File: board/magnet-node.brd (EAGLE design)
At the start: 22.9 x 23.1 mm, 30 parts, among them X1 SMA-142-0701-801/806, X2 SMA-142-0711-821/826

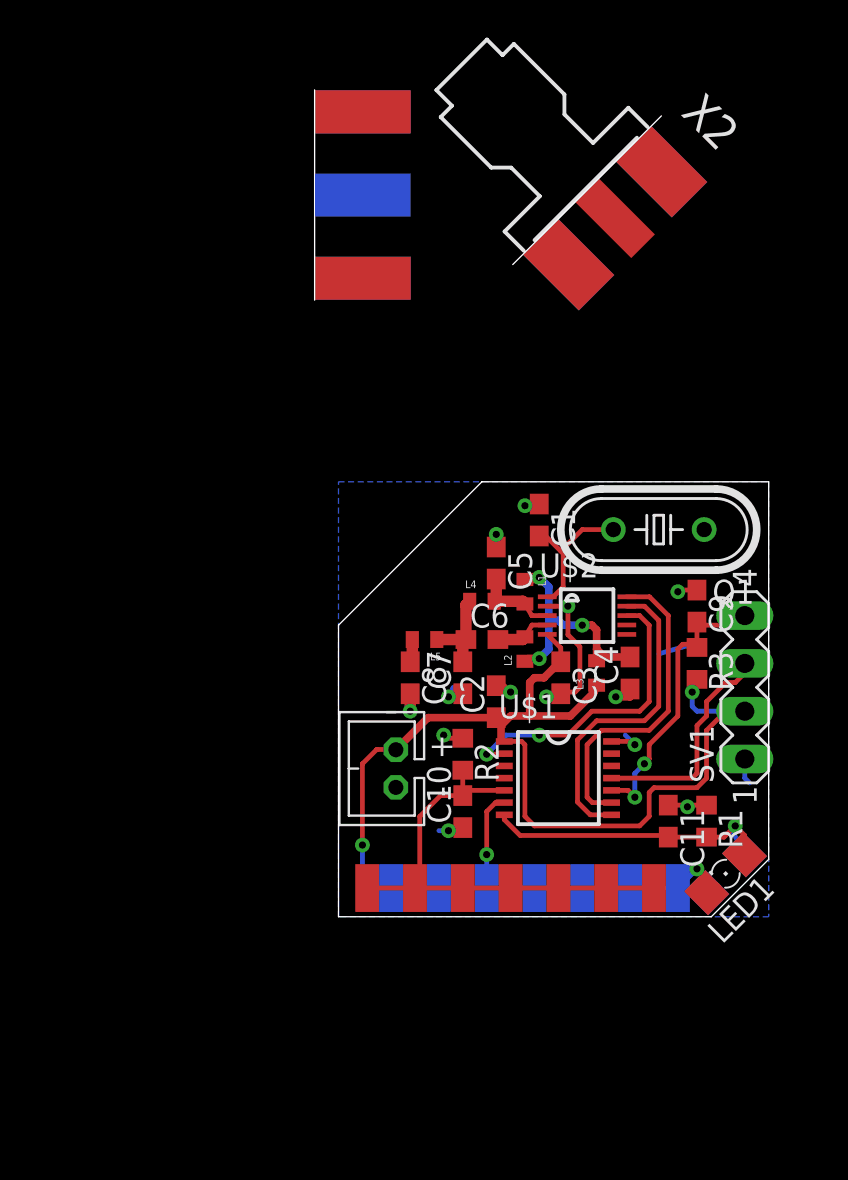
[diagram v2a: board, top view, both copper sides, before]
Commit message: added temp/humid sensor
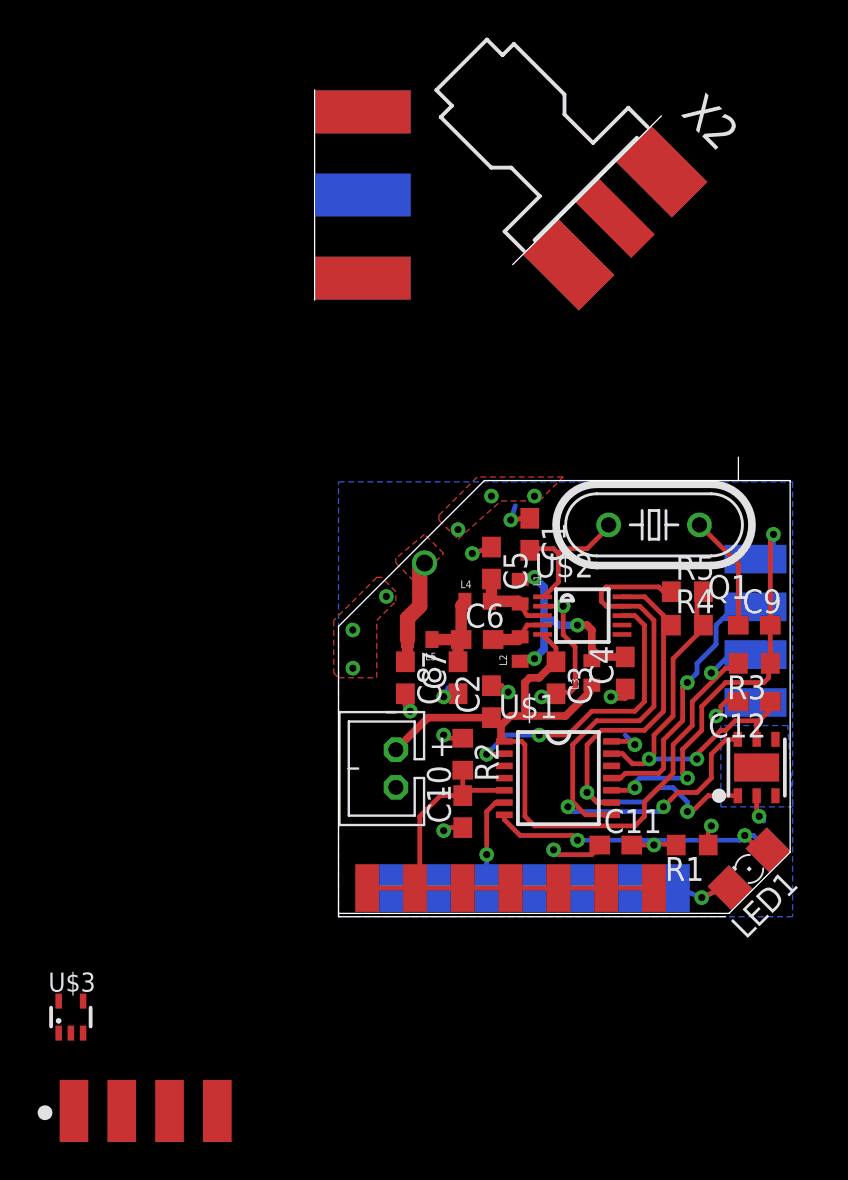
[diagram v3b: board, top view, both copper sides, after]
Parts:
- added C12: (no value), rcl:C0603
- added IC1: HTU21D, Mine:DFN6-L
- added R4, R5: (no value), rcl:R0603
- added SV4: (no value), Mine:EDGE_4
- added U$3: LMT85, Mine:SC70-5L
- SV1: device con-lstb:MA04-1 -> Mine:EDGE_4
- moved C9 3.21 mm to (22.1, 20.1), turned to 0 degrees
- moved C11 3.07 mm to (14.7, 8.38), turned to 0 degrees
- moved SV1 3.06 mm to (22.2, 19.8), flipped to the bottom
- moved R3 3.05 mm to (22.1, 18.0), turned to 180 degrees
- moved R1 1.48 mm to (18.8, 8.38), turned to 180 degrees
- moved LED1 1.28 mm to (21.8, 7.11)
- moved LED2 1.28 mm to (21.8, 7.11)
- moved C1 0.91 mm to (10.2, 24.9)
- moved Q1 0.35 mm to (16.8, 25.4)
- moved L1 0.25 mm to (9.65, 21.8)
- moved L2 0.25 mm to (9.65, 18.8)
- moved C6 0.25 mm to (7.37, 19.3)
- moved C7 0.25 mm to (6.35, 17.3)
- moved L4 0.25 mm to (7.37, 21.3)
- moved L5 0.25 mm to (4.32, 19.3)
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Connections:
- removed net N$3: U$1.8, U$2.9
- removed net N$6: U$1.9, U$2.10
- new net N$11: U$1.3
- new net N$14: U$1.4
- new net SCL: IC1.6, R5.1, U$1.8, U$2.9
- new net SDA: IC1.1, R4.1, U$1.9, U$2.10
- new net VCCS2: C12.1, IC1.5, R4.2, R5.2, U$1.13
- net GND: now also C12.2, IC1.2
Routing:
- net SCL: track 0.00 -> 34.6 mm, vias 0 -> 2
- net SDA: track 0.00 -> 26.8 mm, vias 0 -> 2
- net VCCS2: track 0.00 -> 22.1 mm, vias 0 -> 2
- net N$3: track 17.0 -> 0.00 mm
- net N$6: track 17.0 -> 0.00 mm
- net +3V3: track 55.1 -> 45.0 mm, vias 2 -> 1
- net GND: track 24.9 -> 34.0 mm, vias 13 -> 21
- net N$15: track 15.8 -> 23.1 mm, vias 2 -> 3
- net N$10: track 1.23 -> 5.56 mm, vias 0 -> 1
- net N$2: track 11.8 -> 14.2 mm, vias 0 -> 1
- net N$13: track 17.3 -> 19.4 mm, vias 1 -> 3
- net VCCS: track 26.1 -> 26.9 mm
- added copper zone on layer 1, net GND
- added copper zone on layer 1, net N$10
- added copper zone on layer 16, net N$3
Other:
- board size 22.9 x 23.1 mm -> 24 x 24.4 mm

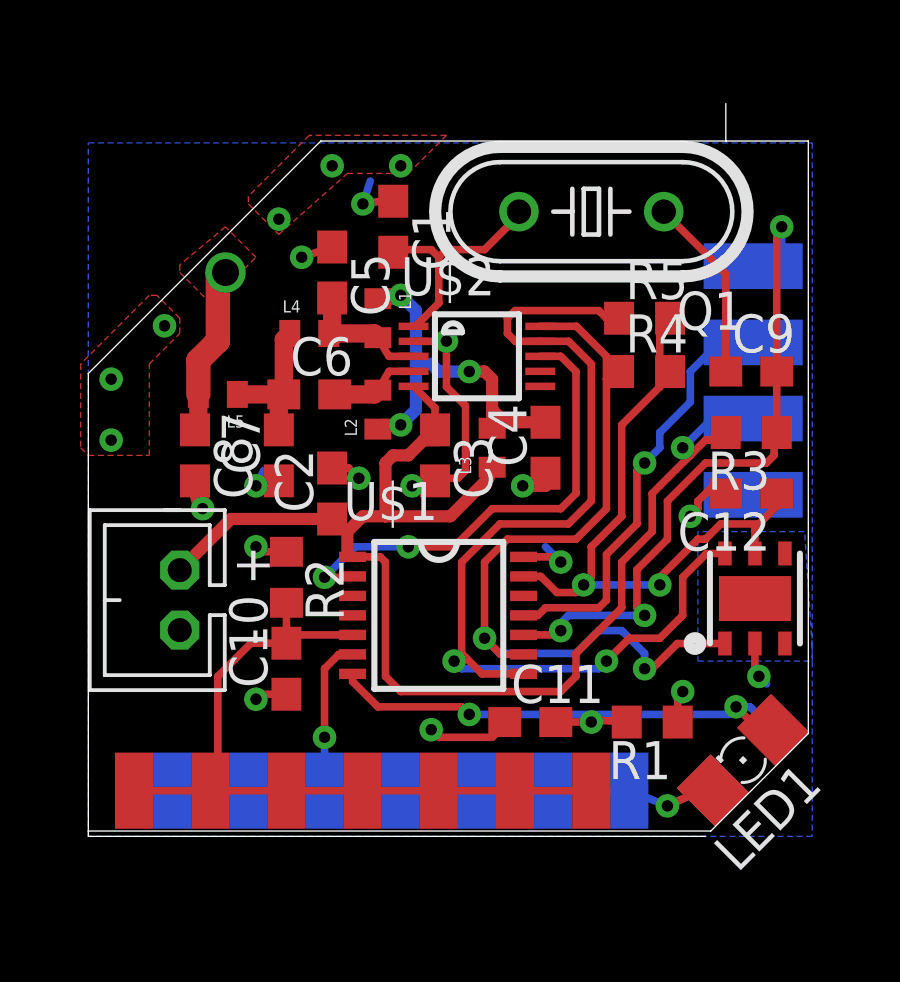
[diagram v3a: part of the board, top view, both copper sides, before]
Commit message: changed footprints in magnet node
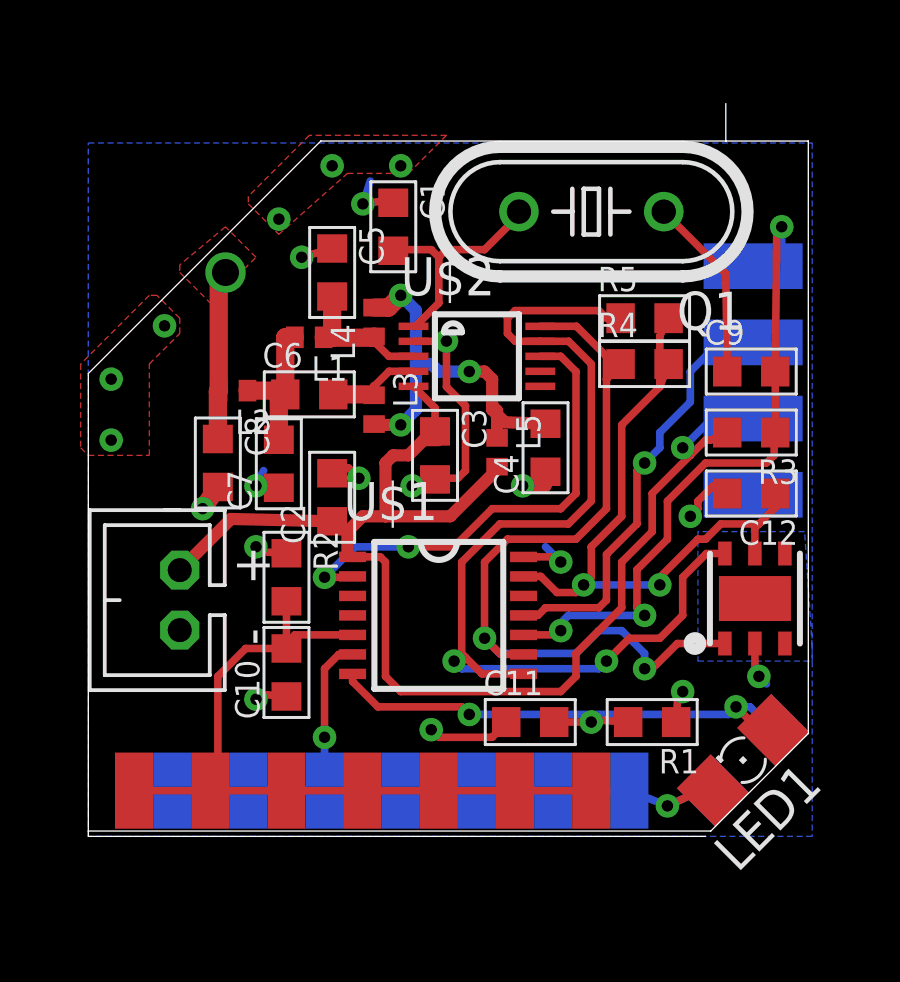
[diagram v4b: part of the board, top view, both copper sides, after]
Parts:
- C1, C10, C11, C12, C2, C3, C4, C5, C6, C7, C8, C9: device rcl:C0603 -> passives-7351:C0603-N
- L1, L2, L3, L4, L5: device SparkFun-Passives:C0402 -> passives-7351:L0402-N
- R1, R2, R3, R4, R5: device rcl:R0603 -> passives-7351:R0603-N
- moved L5 9.50 mm to (13.6, 17.4), turned to 270 degrees
- moved L2 4.87 mm to (4.83, 19.4), turned to 180 degrees
- moved L3 4.14 mm to (9.53, 18.8), turned to 270 degrees
- moved L1 2.37 mm to (7.37, 21.2), turned to 180 degrees
- moved L4 2.19 mm to (9.53, 21.7), turned to 90 degrees
- moved C8 0.80 mm to (4.32, 17.0)
- moved C7 0.28 mm to (6.35, 17.0)
- moved R4 0.25 mm to (18.5, 20.3)
- moved C2 0.13 mm to (8.13, 15.9)
- moved C10 0.12 mm to (6.60, 10.0)
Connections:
- net +3V3: now also L5.2; no longer L3.1
- net N$10: now also L2.2; no longer L5.2
- net N$4: now also L4.2, L5.1; no longer L1.1, L2.1
- net N$7: now also L1.2, L2.1; no longer L4.1, L5.1
- net N$8: now also L1.1, L4.1; no longer L1.2, L4.2
- net N$9: now also L3.1; no longer L2.2
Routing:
- net N$4: track 12.7 -> 13.4 mm

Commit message: adding some values and labels
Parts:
- C4, C5: value (none) -> 2.4p
- C6: value (none) -> 1.2p
- C7, C8: value (none) -> 5.1p
- L1: value (none) -> 30n
- L2: value (none) -> 6.8n
- L3, L4: value (none) -> 3.6n
- L5: value (none) -> 120n
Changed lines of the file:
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@@
 <element name="C1" library="passives-7351" package="C0603-N" value="" x="10.164" y="24.892" rot="R270"/>
 <element name="J2" library="dtb" package="JST-2-TH" value="" x="3.048" y="12.446" rot="R90"/>
-<element name="C4" library="passives-7351" package="C0603-N" value="" x="15.24" y="17.526" rot="R90"/>
-<element name="C5" library="passives-7351" package="C0603-N" value="" x="8.128" y="23.368" rot="R270"/>
-<element name="C6" library="passives-7351" package="C0603-N" value="" x="7.366" y="19.304"/>
-<element name="C7" library="passives-7351" package="C0603-N" value="" x="6.35" y="16.9926" rot="R90"/>
-<element name="C8" library="passives-7351" package="C0603-N" value="" x="4.318" y="17.018" rot="R270"/>
+<element name="C4" library="passives-7351" package="C0603-N" value="2.4p" x="15.24" y="17.526" rot="R90"/>
+<element name="C5" library="passives-7351" package="C0603-N" value="2.4p" x="8.128" y="23.368" rot="R270"/>
+<element name="C6" library="passives-7351" package="C0603-N" value="1.2p" x="7.366" y="19.304"/>
+<element name="C7" library="passives-7351" package="C0603-N" value="5.1p" x="6.35" y="16.9926" rot="R90"/>
+<element name="C8" library="passives-7351" package="C0603-N" value="5.1p" x="4.318" y="17.018" rot="R270"/>
 <element name="X1" library="con-coax" package="J502-ND-142-0701-801/806" value="SMA-142-0701-801/806" x="-1.27" y="42.926" rot="MR180">
 <attribute name="OC_NEWARK" value="90F2624" x="41.91" y="53.086" size="1.778" layer="28" rot="MR180" display="off"/>
@@
 <element name="R4" library="passives-7351" package="R0603-N" value="" x="18.542" y="20.316"/>
 <element name="R5" library="passives-7351" package="R0603-N" value="" x="18.542" y="21.844"/>
-<element name="L1" library="passives-7351" package="L0402-N" value="" x="7.366" y="21.209" rot="R180"/>
-<element name="L2" library="passives-7351" package="L0402-N" value="" x="4.826" y="19.431" rot="R180"/>
-<element name="L3" library="passives-7351" package="L0402-N" value="" x="9.525" y="18.796" rot="R270"/>
-<element name="L4" library="passives-7351" package="L0402-N" value="" x="9.525" y="21.717" rot="R90"/>
-<element name="L5" library="passives-7351" package="L0402-N" value="" x="13.625" y="17.375" rot="R270"/>
+<element name="L1" library="passives-7351" package="L0402-N" value="30n" x="7.366" y="21.209" rot="R180"/>
+<element name="L2" library="passives-7351" package="L0402-N" value="6.8n" x="4.826" y="19.431" rot="R180"/>
+<element name="L3" library="passives-7351" package="L0402-N" value="3.6n" x="9.525" y="18.796" rot="R270"/>
+<element name="L4" library="passives-7351" package="L0402-N" value="3.6n" x="9.525" y="21.717" rot="R90"/>
+<element name="L5" library="passives-7351" package="L0402-N" value="120n" x="13.625" y="17.375" rot="R270"/>
 </elements>
 <signals>

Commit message: small changes
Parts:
- removed SV4: (no value), Mine:EDGE_4
- added TP1, TP4: TPTP14SQ, testpad:TP14SQ
- L5: device passives-7351:L0402-N -> passives-7351:L0603-N
- moved R2 4.96 mm to (5.46, 8.38), turned to 180 degrees
- moved C10 4.62 mm to (2.29, 8.38), turned to 0 degrees
- moved L5 0.29 mm to (13.3, 17.4)
- moved C3 0.13 mm to (11.6, 17.4)
- moved C4 0.13 mm to (15.2, 17.4)
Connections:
- net N$11: now also TP1.TP
- net N$14: now also TP4.TP
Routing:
- net N$11: track 0.00 -> 2.76 mm
- net N$14: track 0.00 -> 2.51 mm
- net N$12: track 26.0 -> 25.1 mm
- net N$4: track 13.4 -> 12.9 mm

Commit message: removed power control from dht
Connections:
- net +3V3: now also C12.1, IC1.5, R4.2, R5.2
- net VCCS2: no longer C12.1, IC1.5, R4.2, R5.2
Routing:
- net VCCS2: track 22.3 -> 11.6 mm
- net +3V3: track 45.3 -> 49.8 mm
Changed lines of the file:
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@@
 <contactref element="L5" pad="2"/>
 <wire x1="13.335" y1="16.599" x2="13.625" y2="16.8" width="0.4064" layer="1"/>
+<contactref element="R4" pad="2"/>
+<contactref element="R5" pad="2"/>
+<contactref element="C12" pad="1"/>
+<contactref element="IC1" pad="5"/>
+<wire x1="19.342" y1="21.844" x2="19.342" y2="20.316" width="0.254" layer="1"/>
+<wire x1="19.342" y1="20.316" x2="19.342" y2="17.996" width="0.254" layer="1"/>
+<wire x1="19.342" y1="17.996" x2="19.812" y2="17.526" width="0.254" layer="1"/>
+<wire x1="22.22" y1="14" x2="22.898" y2="16.002" width="0" layer="19" extent="1-1"/>
+<wire x1="22.16" y1="18.498" x2="22.898" y2="16.002" width="0" layer="19" extent="1-16"/>
 </signal>
 <signal name="N$2">
@@
 <signal name="VCCS2">
 <contactref element="U$1" pad="13"/>
-<contactref element="C12" pad="1"/>
-<contactref element="IC1" pad="5"/>
 <wire x1="14.509" y1="13.238" x2="15.083" y2="13.238" width="0.254" layer="1"/>
 <wire x1="15.083" y1="13.238" x2="15.621" y2="12.7" width="0.254" layer="1"/>
@@
 <via x="19.05" y="12.954" extent="1-16" drill="0.381" shape="octagon"/>
 <wire x1="21.082" y1="14.986" x2="22.352" y2="14.986" width="0.254" layer="1"/>
-<wire x1="22.898" y1="16.002" x2="22.948" y2="15.582" width="0.254" layer="1"/>
 <wire x1="22.948" y1="15.582" x2="22.352" y2="14.986" width="0.254" layer="1"/>
-<wire x1="22.22" y1="14" x2="22.22" y2="14.854" width="0.254" layer="1"/>
 <wire x1="22.22" y1="14.854" x2="22.352" y2="14.986" width="0.254" layer="1"/>
 <wire x1="21.082" y1="14.986" x2="20.574" y2="14.478" width="0.254" layer="1"/>
@@
 <wire x1="20.32" y1="14.478" x2="19.05" y2="13.208" width="0.254" layer="1"/>
 <wire x1="19.05" y1="13.208" x2="19.05" y2="12.954" width="0.254" layer="1"/>
-<contactref element="R4" pad="2"/>
-<contactref element="R5" pad="2"/>
-<wire x1="19.05" y1="19.558" x2="17.78" y2="18.288" width="0.254" layer="1"/>
-<wire x1="17.78" y1="18.288" x2="17.78" y2="15.24" width="0.254" layer="1"/>
-<wire x1="17.78" y1="15.24" x2="16.764" y2="14.224" width="0.254" layer="1"/>
 <wire x1="16.764" y1="14.224" x2="16.764" y2="13.208" width="0.254" layer="1"/>
 <wire x1="16.764" y1="13.208" x2="16.51" y2="12.954" width="0.254" layer="1"/>
-<wire x1="19.05" y1="19.558" x2="19.05" y2="21.248" width="0.254" layer="1"/>
-<wire x1="19.05" y1="21.248" x2="19.342" y2="21.844" width="0.254" layer="1"/>
-<wire x1="19.342" y1="20.316" x2="19.05" y2="19.558" width="0.254" layer="1"/>
 </signal>
 <signal name="N$3">

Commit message: almost ready to do
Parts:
- removed SV1: (no value), Mine:EDGE_4
- removed TP1, TP4: TPTP14SQ, testpad:TP14SQ
- removed U$3: LMT85, Mine:SC70-5L
- removed X1: SMA-142-0701-801/806, con-coax:J502-ND-142-0701-801/806
- removed X2: SMA-142-0711-821/826, con-coax:J502-ND-142-0711-821/826
- added IC2: HTU21D, Mine:DFN6-L
- C1, C2, C3: value (none) -> 100n
- C10: value (none) -> 47n
- C11: value (none) -> 2.4p
- C12: value (none) -> 14p
- C4: value 2.4p -> (none)
- C5: value 2.4p -> 5.1p
- C6: value 1.2p -> 5.1p
- C7: value 5.1p -> 1u
- C8: value 5.1p -> 2.4p
- C9: value (none) -> 1.2p
- IC1: value HTU21D -> MSP430G2X21; device Mine:DFN6-L -> Mine:TSSOP14
- L1: value 30n -> 120n; device passives-7351:L0402-N -> passives-7351:L0603-N
- L2: value 6.8n -> 3.6n
- L3: value 3.6n -> 6.8n
- L4: value 3.6n -> 30n
- L5: value 120n -> 3.6n; device passives-7351:L0603-N -> passives-7351:L0402-N
- R1: value (none) -> 47k
- R2: value (none) -> 1M
- R3: value (none) -> 22k
- R4, R5: value (none) -> 4k7
- SV3: device Mine:MA07-1-SMD -> Mine:EDGE_4
- U$1: value MSP430G2X21 -> MA06-1; device Mine:TSSOP14 -> Mine:MA06-1-SMD
- moved C10 23.0 mm to (22.1, 20.1)
- moved SV3 18.9 mm to (22.2, 19.8), flipped to the bottom, turned to 90 degrees
- moved C1 17.8 mm to (3.56, 8.38), turned to 0 degrees
- moved C11 16.4 mm to (8.13, 23.4), turned to 270 degrees
- moved C12 14.9 mm to (10.2, 24.9), turned to 270 degrees
- moved C9 14.8 mm to (7.37, 19.3)
- moved R2 12.8 mm to (18.3, 8.38)
- moved R1 12.1 mm to (6.73, 8.38)
- moved C8 10.9 mm to (15.2, 17.4), turned to 90 degrees
- moved IC1 10.6 mm to (11.7, 11.9)
- moved C2 9.99 mm to (14.7, 8.38), turned to 0 degrees
- moved L1 7.08 mm to (13.3, 17.4), turned to 270 degrees
- moved C4 7.00 mm to (22.1, 16.0), turned to 180 degrees
- moved C5 6.62 mm to (6.35, 17.0), turned to 90 degrees
- moved U$1 5.84 mm to (11.7, 6.10)
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- renumbered J2 to J1, U$2 to IC3
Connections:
- removed net N$11: TP1.TP, U$1.3
- removed net N$14: TP4.TP, U$1.4
- new net IO1: IC1.3, SV2.6
- new net IO2: IC1.4, SV2.5
- net +3V3: now also C4.1, C7.1, IC1.1, IC2.5, L1.2, SV3.2; no longer C12.1, C2.1, IC1.5, L5.2, SV1.2, U$1.1
- net GND: now also C12.1, C2.1, C4.2, C6.2, C7.2, C8.1, IC1.14, IC2.2, SV2.7, SV3.1; no longer C12.2, C2.2, C4.1, C7.1, C8.2, C9.1, IC1.2, SV1.1, U$1.14, X1.G@1, X1.G@2, X1.G@3, X1.G@4
- net N$1: now also IC1.2; no longer U$1.2
- net N$10: now also C6.1, L3.2; no longer C8.1, L2.2, X1.1
- net N$12: now also C1.2, IC1.5, R1.2, U$1.1, U$1.2, U$1.3, U$1.4, U$1.6; no longer C10.2, R2.2, SV3.1, SV3.2, SV3.3, SV3.4, SV3.5, SV3.6, SV3.7
- net N$13: now also C2.2, IC1.7, R2.2; no longer C11.2, R1.2, U$1.7
- net N$15: now also C10.2, IC1.10, SV3.4; no longer C9.2, SV1.4, U$1.10
- net N$2: now also IC1.11, SV3.3; no longer SV1.3, U$1.11
- net N$4: now also C8.2, L1.1, L2.2, L5.2; no longer C4.2, L3.2, L4.2, L5.1
- net N$5: now also C12.2; no longer C1.2
- net N$7: now also C5.2, C9.1, L3.1, L4.2; no longer C6.1, C7.2, L1.2, L2.1
- net N$8: now also C11.2, L5.1; no longer C5.2, L1.1
- net N$9: now also C9.2, L2.1; no longer C6.2, L3.1
- net SCL: now also IC1.8, IC2.6; no longer IC1.6, U$1.8
- net SDA: now also IC1.9, IC2.1; no longer IC1.1, U$1.9
- net VCCS: now also IC1.6; no longer SV2.5, SV2.6, SV2.7, U$1.6
- net VCCS2: now also IC1.13; no longer U$1.13
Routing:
- net VCCS2: track 11.6 -> 0.00 mm, vias 2 -> 0
- net IO2: track 0.00 -> 10.7 mm, vias 0 -> 1
- net IO1: track 0.00 -> 10.5 mm, vias 0 -> 1
- net +3V3: track 49.8 -> 59.3 mm
- net VCCS: track 26.9 -> 20.8 mm
- net N$12: track 25.1 -> 21.7 mm
- net N$11: track 2.76 -> 0.00 mm
- net GND: track 34.1 -> 36.7 mm, vias 21 -> 22
- net N$14: track 2.51 -> 0.00 mm
- net N$15: track 23.1 -> 21.3 mm
- net N$13: track 19.5 -> 18.9 mm
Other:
- board size 24 x 24.4 mm -> 24 x 23 mm
- board text added: "GND"
- board text added: "IO1"
- board text added: "IO2"
- board text added: "Matt Brejza Jan 2015"
- board text added: "RST"
- board text added: "TST"
- board text added: "V"
- board text added: "VCC"
- board text added: "©"
